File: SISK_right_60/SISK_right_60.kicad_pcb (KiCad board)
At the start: 2 copper layers, 194.5 x 121.8 mm, 76 parts, among them J1 OLED_128x32, J2 Battery Conn, J3 alternative on/off SW (wired), SW1 "6", SW10 "Z", SW11 "U", SW12 "I", SW13 "O", SW14 "P", SW15 "Ü", SW16 "*", SW19 "H", SW2 "7", SW20 "J", SW21 "K", SW22 "L", SW23 "Ö", SW24 "Ä", SW25 "'", SW27 "N", SW28 "M", SW29 ";", SW3 "8", SW30 ":", SW31 "-", SW32 "shift_R", SW35 "SPACE_R", SW36 "Alt", SW37 FN, SW38 "Ctrl", SW39 FN2, SW4 "9", SW5 "0", SW6 "ß", SW7 "`", SW8 "Backspace", SW9 "Enter", U1 Nice_Nano_V2

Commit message: fixed most of issues, updated 60% version
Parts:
- removed SW39: FN2, ScottoKeebs_Hotswap:Hotswap_MX_Plated_1.25u
- added R1: 5K, Resistor_SMD:R_1206_3216Metric_Pad1.30x1.75mm_HandSolder, B.Cu at (86.7, 51.8)
- added R2: 5K, Resistor_SMD:R_1206_3216Metric_Pad1.30x1.75mm_HandSolder, B.Cu at (89.2, 51.8)
- added REF05: MountingHole_3.2mm_M3_ISO7380, MountingHole:MountingHole_3.2mm_M3_ISO7380, F.Cu at (190.6, 131.7)
- added SW17: SW_push, MX_Hotswap:MX-Hotswap-1.25U, B.Cu at (178.7, 141.2)
- J2: value Battery Conn -> Conn
- J3: value alternative on/off SW (wired) -> SWITCH
- SW-ONOFF-01: value onboard ON/OFF SW -> ~
- SW1: value "6" -> SW_push; footprint ScottoKeebs_Hotswap:Hotswap_MX_Plated_1.00u -> MX_Hotswap:MX-Hotswap-1U; moved to B.Cu
- SW10: value "Z" -> SW_push; footprint ScottoKeebs_Hotswap:Hotswap_MX_Plated_1.00u -> MX_Hotswap:MX-Hotswap-1U; moved to B.Cu
- SW11: value "U" -> SW_push; footprint ScottoKeebs_Hotswap:Hotswap_MX_Plated_1.00u -> MX_Hotswap:MX-Hotswap-1U; moved to B.Cu
- SW12: value "I" -> SW_push; footprint ScottoKeebs_Hotswap:Hotswap_MX_Plated_1.00u -> MX_Hotswap:MX-Hotswap-1U; moved to B.Cu
- SW13: value "O" -> SW_push; footprint ScottoKeebs_Hotswap:Hotswap_MX_Plated_1.00u -> MX_Hotswap:MX-Hotswap-1U; moved to B.Cu
- SW14: value "P" -> SW_push; footprint ScottoKeebs_Hotswap:Hotswap_MX_Plated_1.00u -> MX_Hotswap:MX-Hotswap-1U; moved to B.Cu
- SW15: value "Ü" -> SW_push; footprint ScottoKeebs_Hotswap:Hotswap_MX_Plated_1.00u -> MX_Hotswap:MX-Hotswap-1U; moved to B.Cu
- SW16: value "*" -> SW_push; footprint ScottoKeebs_Hotswap:Hotswap_MX_Plated_1.00u -> MX_Hotswap:MX-Hotswap-1U; moved to B.Cu
- SW19: value "H" -> SW_push; footprint ScottoKeebs_Hotswap:Hotswap_MX_Plated_1.00u -> MX_Hotswap:MX-Hotswap-1U; moved to B.Cu
- SW2: value "7" -> SW_push; footprint ScottoKeebs_Hotswap:Hotswap_MX_Plated_1.00u -> MX_Hotswap:MX-Hotswap-1U; moved to B.Cu
- SW20: value "J" -> SW_push; footprint ScottoKeebs_Hotswap:Hotswap_MX_Plated_1.00u -> MX_Hotswap:MX-Hotswap-1U; moved to B.Cu
- SW21: value "K" -> SW_push; footprint ScottoKeebs_Hotswap:Hotswap_MX_Plated_1.00u -> MX_Hotswap:MX-Hotswap-1U; moved to B.Cu
- SW22: value "L" -> SW_push; footprint ScottoKeebs_Hotswap:Hotswap_MX_Plated_1.00u -> MX_Hotswap:MX-Hotswap-1U; moved to B.Cu
- SW23: value "Ö" -> SW_push; footprint ScottoKeebs_Hotswap:Hotswap_MX_Plated_1.00u -> MX_Hotswap:MX-Hotswap-1U; moved to B.Cu
- SW24: value "Ä" -> SW_push; footprint ScottoKeebs_Hotswap:Hotswap_MX_Plated_1.00u -> MX_Hotswap:MX-Hotswap-1U; moved to B.Cu
- SW25: value "'" -> SW_push; footprint ScottoKeebs_Hotswap:Hotswap_MX_Plated_1.00u -> MX_Hotswap:MX-Hotswap-1U; moved to B.Cu
- SW27: value "N" -> SW_push; footprint ScottoKeebs_Hotswap:Hotswap_MX_Plated_1.00u -> MX_Hotswap:MX-Hotswap-1U; moved to B.Cu
- SW28: value "M" -> SW_push; footprint ScottoKeebs_Hotswap:Hotswap_MX_Plated_1.00u -> MX_Hotswap:MX-Hotswap-1U; moved to B.Cu
- SW29: value ";" -> SW_push; footprint ScottoKeebs_Hotswap:Hotswap_MX_Plated_1.00u -> MX_Hotswap:MX-Hotswap-1U; moved to B.Cu
- SW3: value "8" -> SW_push; footprint ScottoKeebs_Hotswap:Hotswap_MX_Plated_1.00u -> MX_Hotswap:MX-Hotswap-1U; moved to B.Cu
- SW30: value ":" -> SW_push; footprint ScottoKeebs_Hotswap:Hotswap_MX_Plated_1.00u -> MX_Hotswap:MX-Hotswap-1U; moved to B.Cu
- SW31: value "-" -> SW_push; footprint ScottoKeebs_Hotswap:Hotswap_MX_Plated_1.00u -> MX_Hotswap:MX-Hotswap-1U; moved to B.Cu
- SW32: value "shift_R" -> SW_push; footprint ScottoKeebs_Hotswap:Hotswap_MX_Plated_2.75u -> MX_Hotswap:MX-Hotswap-2.75U; moved to B.Cu
- SW35: value "SPACE_R" -> SW_push; footprint ScottoKeebs_Hotswap:Hotswap_MX_Plated_2.75u -> MX_Hotswap:MX-Hotswap-2.75U; moved to B.Cu
- SW36: value "Alt" -> SW_push; footprint ScottoKeebs_Hotswap:Hotswap_MX_Plated_1.25u -> MX_Hotswap:MX-Hotswap-1.25U; moved to B.Cu
- SW37: value FN -> SW_push; footprint ScottoKeebs_Hotswap:Hotswap_MX_Plated_1.25u -> MX_Hotswap:MX-Hotswap-1.25U; moved to B.Cu
- SW38: value "Ctrl" -> SW_push; footprint ScottoKeebs_Hotswap:Hotswap_MX_Plated_1.25u -> MX_Hotswap:MX-Hotswap-1.25U; moved to B.Cu
- SW4: value "9" -> SW_push; footprint ScottoKeebs_Hotswap:Hotswap_MX_Plated_1.00u -> MX_Hotswap:MX-Hotswap-1U; moved to B.Cu
- SW5: value "0" -> SW_push; footprint ScottoKeebs_Hotswap:Hotswap_MX_Plated_1.00u -> MX_Hotswap:MX-Hotswap-1U; moved to B.Cu
- SW6: value "ß" -> SW_push; footprint ScottoKeebs_Hotswap:Hotswap_MX_Plated_1.00u -> MX_Hotswap:MX-Hotswap-1U; moved to B.Cu
- SW7: value "`" -> SW_push; footprint ScottoKeebs_Hotswap:Hotswap_MX_Plated_1.00u -> MX_Hotswap:MX-Hotswap-1U; moved to B.Cu
- SW8: value "Backspace" -> SW_push; footprint ScottoKeebs_Hotswap:Hotswap_MX_Plated_2.00u -> MX_Hotswap:MX-Hotswap-2U; moved to B.Cu
- SW9: value "Enter" -> SW_push; footprint ScottoKeebs_Hotswap:Hotswap_MX_Plated_ISOEnter -> MX_Hotswap:MX-Hotswap-ISO; moved to B.Cu
- moved D3 39.5 mm to (212.6, 131.9)
- moved D2 38.4 mm to (190.8, 111.6)
- moved D1 18.0 mm to (200.0, 74.9)
- moved D25 16.0 mm to (166.6, 132.3)
- moved D8 7.35 mm to (71.1, 134.0)
- moved D19 7.09 mm to (162.0, 114.6)
- moved D30 2.02 mm to (142.9, 132.1)
- moved D39 1.85 mm to (87.6, 114.6)
- moved D35 1.60 mm to (119.1, 132.3)
- moved REF01 0.16 mm to (62.0, 73.7)
- turned SW1 to 180 degrees
- turned SW10 to 180 degrees
- turned SW11 to 180 degrees
- turned SW12 to 180 degrees
- turned SW13 to 180 degrees
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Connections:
- net +3.3V renamed +BATT
- net Net-(J1-SCL) renamed /SCL
- net Net-(J1-SDA) renamed /SDA
- net Net-(J3-Pin_1) renamed +VDC
- net VCC renamed +3,3V
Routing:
- net /ROW3: track 295.5 -> 257.5 mm
- net Net-(D2-A): track 10.2 -> 44.6 mm
- net /COL4: track 212.3 -> 183.9 mm, vias 0 -> 5
- net Net-(D8-A): track 17.8 -> 44.4 mm
- net Net-(D25-A): track 83.8 -> 60.6 mm
- net /COL5: track 226.6 -> 206.0 mm, vias 0 -> 6
- net Net-(D3-A): track 10.3 -> 29.2 mm
- net +3,3V: track 30.1 -> 47.4 mm
- net /SCL: track 34.4 -> 50.9 mm
- net /COL3: track 180.4 -> 165.0 mm, vias 0 -> 5
- net Net-(D1-A): track 6.92 -> 21.5 mm
- net Net-(D19-A): track 21.9 -> 36.2 mm
- net /COL2: track 171.3 -> 159.3 mm, vias 1 -> 6
- net /SDA: track 30.8 -> 42.5 mm
- net /ROW4: track 294.6 -> 284.3 mm, vias 3 -> 1
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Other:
- board size 194.5 x 121.8 mm -> 175.4 x 121.8 mm

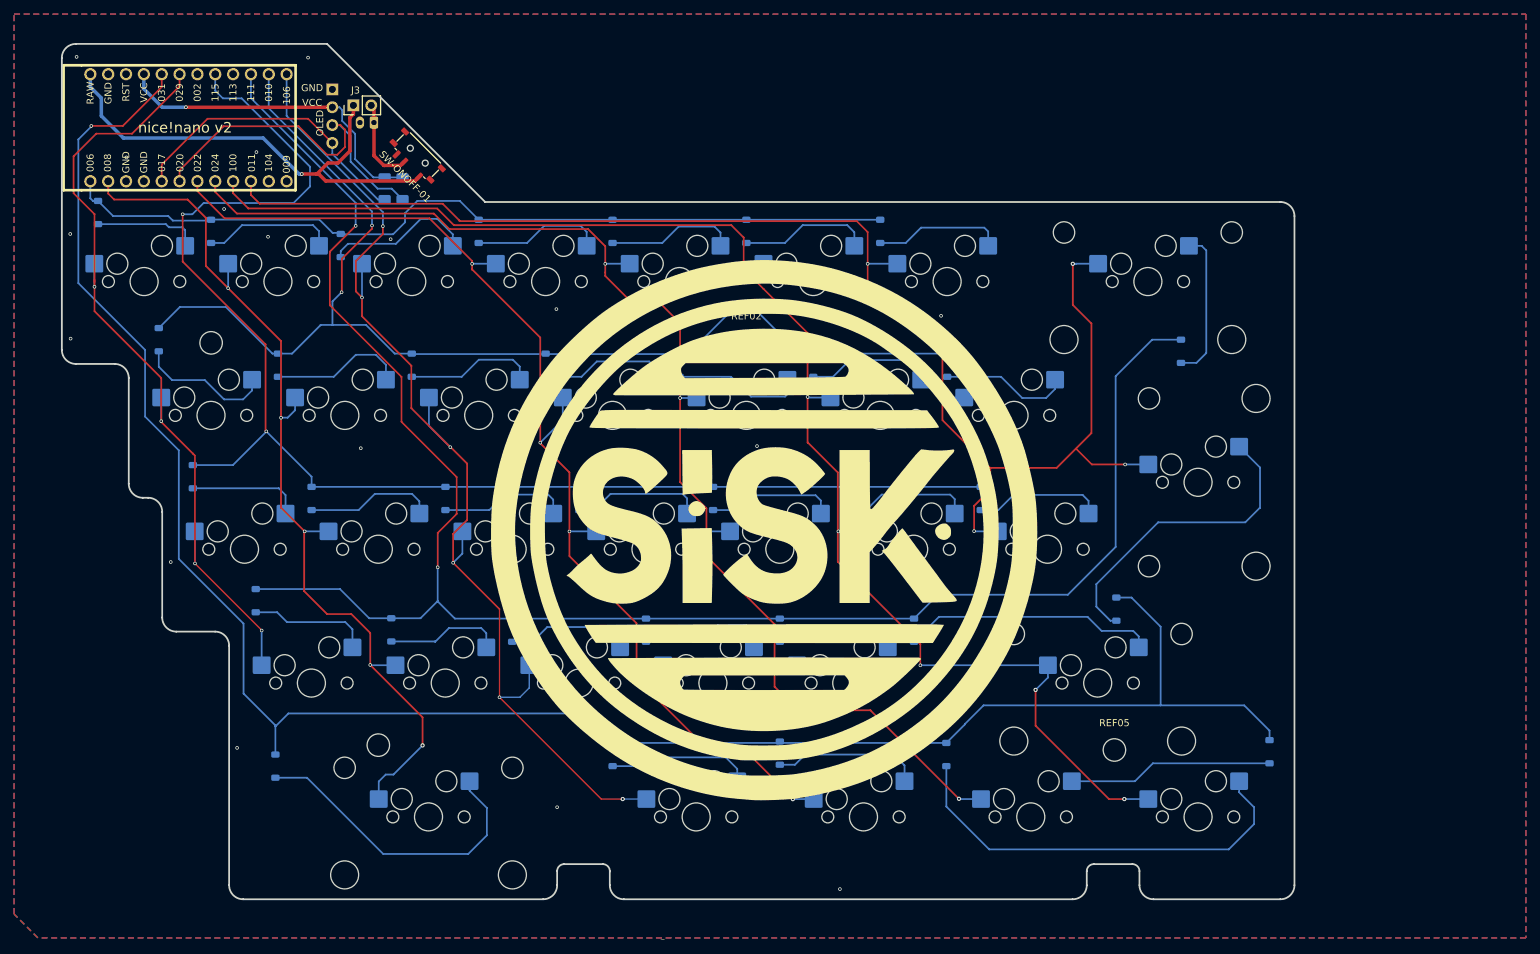
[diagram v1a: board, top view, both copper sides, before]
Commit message: improved the whole mounting hole situation
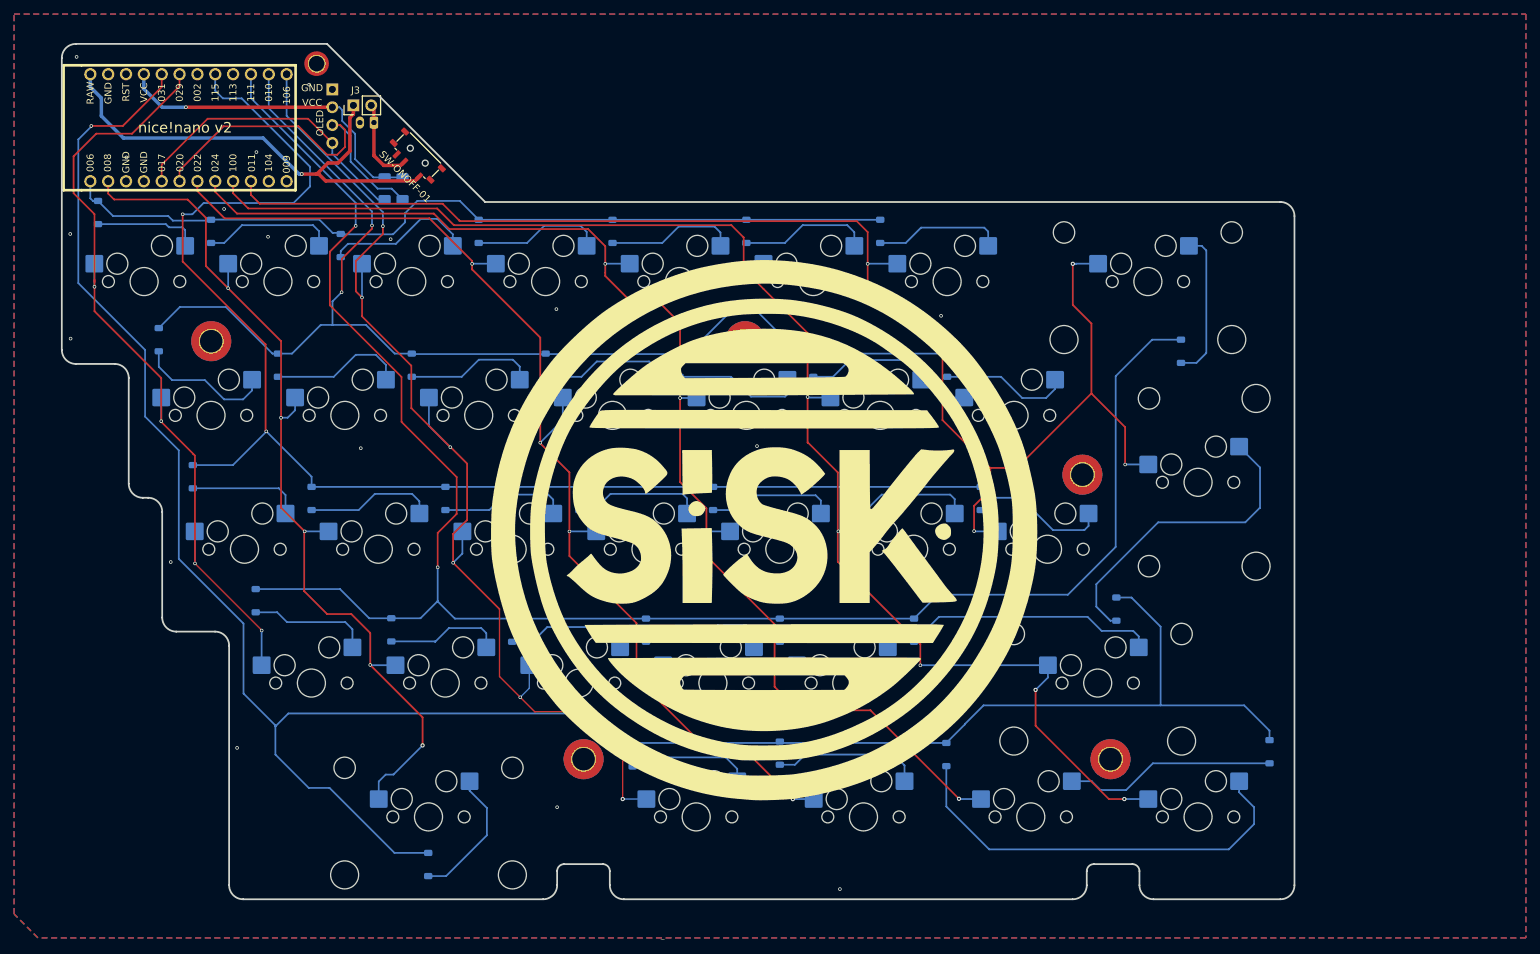
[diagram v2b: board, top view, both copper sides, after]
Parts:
- removed REF01, REF02, REF04, REF05: MountingHole_3.2mm_M3_ISO7380, MountingHole:MountingHole_3.2mm_M3_ISO7380
- added H1: M3, MountingHole:MountingHole_3.2mm_M3_ISO7380_Pad_TopBottom, F.Cu at (115.0, 133.0)
- added H2: M3, MountingHole:MountingHole_3.2mm_M3_ISO7380_Pad_TopBottom, F.Cu at (190.0, 133.0)
- added H3: M3, MountingHole:MountingHole_3.2mm_M3_ISO7380_Pad_TopBottom, F.Cu at (186.0, 92.5)
- added H4: M3, MountingHole:MountingHole_3.2mm_M3_ISO7380_Pad_TopBottom, F.Cu at (138.0, 73.5)
- added H5: M3, MountingHole:MountingHole_3.2mm_M3_ISO7380_Pad_TopBottom, F.Cu at (62.0, 73.5)
- added H6: M2, MountingHole:MountingHole_2.2mm_M2_ISO7380_Pad_TopOnly, F.Cu at (77.0, 34.0)
- moved D8 25.9 mm to (92.9, 148.0)
- moved D35 2.85 mm to (122.0, 132.4)
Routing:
- net /ROW4: track 284.3 -> 311.9 mm
- net Net-(D8-A): track 44.4 -> 19.5 mm
- net Net-(D35-A): track 20.7 -> 17.9 mm
- net Net-(D13-A): track 18.4 -> 20.0 mm
- net Net-(D3-A): track 29.2 -> 30.2 mm
- net /COL6: track 209.9 -> 210.8 mm

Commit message: last changes on silkscreen before manufaturing
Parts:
- moved J3 0.59 mm to (82.1, 39.4)
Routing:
- net +BATT: track 12.5 -> 13.1 mm
- net +VDC: track 68.9 -> 69.5 mm
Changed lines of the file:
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@@
 			(unlocked yes)
 			(layer "F.SilkS")
+			(hide yes)
 			(effects
 				(font
@@
 		)
 		(property "Label" "onboard ON/OFF SW"
-			(at 0 0 -45)
+			(at 0.169706 2.722361 -45)
 			(unlocked yes)
-			(layer "F.Fab")
-			(hide yes)
+			(layer "F.SilkS")
 			(effects
 				(font
-					(size 1.5 1.5)
-					(thickness 0.2)
+					(size 1 1)
+					(thickness 0.15)
 				)
 			)
@@
 		(locked yes)
 		(layer "F.Cu")
-		(at 82.235 39.94 90)
+		(at 82.102 39.361 90)
 		(descr "Through hole straight pin header, 1x02, 2.54mm pitch, single row")
 		(tags "Through hole pin header THT 1x02 2.54mm single row")
@@
 			)
 		)
-		(property "Label" "Fn2"
-			(at 0 0 180)
+		(property "Label" "Super"
+			(at 0 -4.445 0)
 			(unlocked yes)
-			(layer "B.Fab")
-			(hide yes)
+			(layer "B.SilkS")
 			(effects
 				(font
@@
 		)
 		(property "Label" "Shift R"
-			(at 0 0 180)
+			(at 0 -4.445 0)
 			(unlocked yes)
-			(layer "B.Fab")
-			(hide yes)
+			(layer "B.SilkS")
 			(effects
 				(font
@@
 		)
 		(property "Label" "Enter"
-			(at 0 0 180)
+			(at -0.15875 -5.08 0)
 			(unlocked yes)
-			(layer "B.Fab")
-			(hide yes)
+			(layer "B.SilkS")
 			(effects
 				(font
@@
 		)
 		(property "Label" "H"
-			(at 0 0 180)
+			(at 0 -4.445 180)
 			(unlocked yes)
-			(layer "B.Fab")
-			(hide yes)
+			(layer "B.SilkS")
 			(effects
 				(font
@@
 		)
 		(property "Label" "\";\""
-			(at 0 0 180)
+			(at 0 -4.445 0)
 			(unlocked yes)
-			(layer "B.Fab")
-			(hide yes)
+			(layer "B.SilkS")
 			(effects
 				(font
@@
 		)
 		(property "Label" "Backspace"
-			(at 0 0 180)
+			(at 0.3175 -4.445 0)
 			(unlocked yes)
-			(layer "B.Fab")
-			(hide yes)
+			(layer "B.SilkS")
 			(effects
 				(font
@@
 		)
 		(property "Label" "Space R"
-			(at 0 0 180)
+			(at -6.82625 -3.175 0)
 			(unlocked yes)
-			(layer "B.Fab")
-			(hide yes)
+			(layer "B.SilkS")
 			(effects
 				(font
@@
 			)
 		)
-		(property "Label" "Fn"
-			(at 0 0 180)
+		(property "Label" "Alt"
+			(at 0 -4.445 0)
 			(unlocked yes)
-			(layer "B.Fab")
-			(hide yes)
+			(layer "B.SilkS")
 			(effects
 				(font
@@
 		)
 		(property "Label" "L"
-			(at 0 0 180)
+			(at 0 -4.445 0)
 			(unlocked yes)
-			(layer "B.Fab")
-			(hide yes)
+			(layer "B.SilkS")
 			(effects
 				(font
@@
 		)
 		(property "Label" "0"
-			(at 0 0 180)
+			(at 0 -4.445 0)
 			(unlocked yes)
-			(layer "B.Fab")
-			(hide yes)
+			(layer "B.SilkS")
 			(effects
 				(font
@@
 		)
 		(property "Label" "\"-\""
-			(at 0 0 180)
+			(at 0 -4.445 0)
 			(unlocked yes)
-			(layer "B.Fab")
-			(hide yes)
+			(layer "B.SilkS")
 			(effects
 				(font
@@
 			)
 		)
-		(property "Label" "Alt"
-			(at 0 0 180)
+		(property "Label" "Fn"
+			(at 0 -4.445 0)
 			(unlocked yes)
-			(layer "B.Fab")
-			(hide yes)
+			(layer "B.SilkS")
 			(effects
 				(font
@@
 		)
 		(property "Label" "6"
-			(at 0 0 180)
+			(at 0 -4.445 0)
 			(unlocked yes)
-			(layer "B.Fab")
-			(hide yes)
+			(layer "B.SilkS")
 			(effects
 				(font
@@
 		)
 		(property "Label" "M"
-			(at 0 0 180)
+			(at 0 -4.445 0)
 			(unlocked yes)
-			(layer "B.Fab")
-			(hide yes)
+			(layer "B.SilkS")
 			(effects
 				(font
@@
 		)
 		(property "Label" "J"
-			(at 0 0 180)
+			(at 0 -4.445 0)
 			(unlocked yes)
-			(layer "B.Fab")
-			(hide yes)
+			(layer "B.SilkS")
 			(effects
 				(font
@@
 		)
 		(property "Label" "\"'\""
-			(at 0 0 180)
+			(at 0 -4.445 0)
 			(unlocked yes)
-			(layer "B.Fab")
-			(hide yes)
+			(layer "B.SilkS")
 			(effects
 				(font
@@
 		)
 		(property "Label" "ß"
-			(at 0 0 180)
+			(at 0 -4.445 0)
 			(unlocked yes)
-			(layer "B.Fab")
-			(hide yes)
+			(layer "B.SilkS")
 			(effects
 				(font
@@
 		)
 		(property "Label" "\":\""
-			(at 0 0 180)
+			(at 0 -4.445 0)
 			(unlocked yes)
-			(layer "B.Fab")
-			(hide yes)
+			(layer "B.SilkS")
 			(effects
 				(font
@@
 		)
 		(property "Label" "Ä"
-			(at 0 0 180)
+			(at 0 -4.445 0)
 			(unlocked yes)
-			(layer "B.Fab")
-			(hide yes)
+			(layer "B.SilkS")
 			(effects
 				(font
@@
 		)
 		(property "Label" "9"
-			(at 0 0 180)
+			(at 0 -4.445 0)
 			(unlocked yes)
-			(layer "B.Fab")
-			(hide yes)
+			(layer "B.SilkS")
 			(effects
 				(font
@@
 		(tags "resistor handsolder")
 		(property "Reference" "R2"
-			(at 0 1.82 90)
+			(at 0 -1.63 90)
 			(layer "B.SilkS")
 			(effects
@@
 		)
 		(property "Label" "7"
-			(at 0 0 180)
+			(at 0 -4.445 0)
 			(unlocked yes)
-			(layer "B.Fab")
-			(hide yes)
+			(layer "B.SilkS")
 			(effects
 				(font
@@
 		)
 		(property "Label" "N"
-			(at 0 0 180)
+			(at 0 -4.445 180)
 			(unlocked yes)
-			(layer "B.Fab")
-			(hide yes)
+			(layer "B.SilkS")
 			(effects
 				(font
@@
 		)
 		(property "Label" "8"
-			(at 0 0 180)
+			(at 0 -4.445 0)
 			(unlocked yes)
-			(layer "B.Fab")
-			(hide yes)
+			(layer "B.SilkS")
 			(effects
 				(font
@@
 		)
 		(property "Label" "\"`\""
-			(at 0 0 180)
+			(at 0 -4.445 0)
 			(unlocked yes)
-			(layer "B.Fab")
-			(hide yes)
+			(layer "B.SilkS")
 			(effects
 				(font
@@
 		)
 		(property "Label" "K"
-			(at 0 0 180)
+			(at 0 -4.445 0)
 			(unlocked yes)
-			(layer "B.Fab")
-			(hide yes)
+			(layer "B.SilkS")
 			(effects
 				(font
@@
 		)
 		(property "Label" "Ctrl"
-			(at 0 0 180)
+			(at -0.15875 -4.445 0)
 			(unlocked yes)
-			(layer "B.Fab")
+			(layer "B.SilkS")
 			(effects
 				(font
@@
 		)
 		(property "Label" "Ö"
-			(at 0 0 180)
+			(at 0 -4.445 0)
 			(unlocked yes)
-			(layer "B.Fab")
-			(hide yes)
+			(layer "B.SilkS")
 			(effects
 				(font
@@
 	)
 	(gr_text "+"
-		(at 87.035 52.215 0)
+		(at 88.325 50.41 0)
 		(layer "B.SilkS")
 		(effects
@@
 	)
 	(gr_text "-"
-		(at 83.485 52.115 0)
+		(at 81.975 50.41 0)
 		(layer "B.SilkS")
 		(effects
@@
 	)
 	(gr_text "OLED"
-		(at 78.06 44.34 90)
+		(at 78.06 45.33 90)
 		(layer "F.SilkS")
 		(effects
@@
 	)
 	(segment
-		(start 85.16 40.325)
-		(end 84.775 39.94)
+		(start 85.16 47.09)
+		(end 86.56 48.49)
 		(width 0.5)
 		(layer "F.Cu")
@@
 	)
 	(segment
-		(start 85.16 47.09)
-		(end 86.56 48.49)
+		(start 85.16 42.39)
+		(end 85.16 39.879)
 		(width 0.5)
 		(layer "F.Cu")
@@
 	)
 	(segment
-		(start 89.455456 48.044544)
-		(end 89.455456 47.978883)
-		(width 0.25)
+		(start 85.16 39.879)
+		(end 84.642 39.361)
+		(width 0.5)
 		(layer "F.Cu")
 		(net 43)
 	)
 	(segment
-		(start 88.944339 48.49)
+		(start 89.455456 48.044544)
 		(end 89.455456 47.978883)
-		(width 0.5)
+		(width 0.25)
 		(layer "F.Cu")
 		(net 43)
 	)
 	(segment
-		(start 85.16 42.39)
-		(end 85.16 40.325)
+		(start 88.944339 48.49)
+		(end 89.455456 47.978883)
 		(width 0.5)
 		(layer "F.Cu")
@@
 	)
 	(segment
-		(start 78.61 48.14)
-		(end 80.035 48.14)
-		(width 0.5)
-		(layer "F.Cu")
-		(net 55)
-	)
-	(segment
 		(start 74.885 49.715)
 		(end 77.31 49.715)
@@
 	)
 	(segment
-		(start 81.735 41.69)
-		(end 82.235 41.19)
+		(start 78.61 48.14)
+		(end 80.035 48.14)
 		(width 0.5)
 		(layer "F.Cu")
@@
 	)
 	(segment
-		(start 82.235 41.19)
-		(end 82.235 39.94)
+		(start 77.31 49.715)
+		(end 77.035 49.715)
 		(width 0.5)
 		(layer "F.Cu")
@@
 	(segment
 		(start 77.31 49.715)
-		(end 77.035 49.715)
+		(end 78.285 50.69)
 		(width 0.5)
 		(layer "F.Cu")
@@
 	)
 	(segment
-		(start 77.31 49.715)
-		(end 78.285 50.69)
+		(start 78.285 50.69)
+		(end 90.986981 50.69)
 		(width 0.5)
 		(layer "F.Cu")
@@
 	)
 	(segment
-		(start 77.035 49.715)
-		(end 78.61 48.14)
+		(start 81.735 39.728)
+		(end 82.102 39.361)
 		(width 0.5)
 		(layer "F.Cu")
@@
 	)
 	(segment
-		(start 78.285 50.69)
-		(end 90.986981 50.69)
+		(start 77.035 49.715)
+		(end 78.61 48.14)
 		(width 0.5)
 		(layer "F.Cu")
@@
 	(segment
 		(start 81.735 46.44)
-		(end 81.735 41.69)
+		(end 81.735 39.728)
 		(width 0.5)
 		(layer "F.Cu")
